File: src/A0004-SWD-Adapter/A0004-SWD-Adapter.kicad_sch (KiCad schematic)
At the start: 13 parts, among them P1 LARGE_SBH11-PBPC-D10-RA-BK_1, P2 SMALL_3220-20-0200-00

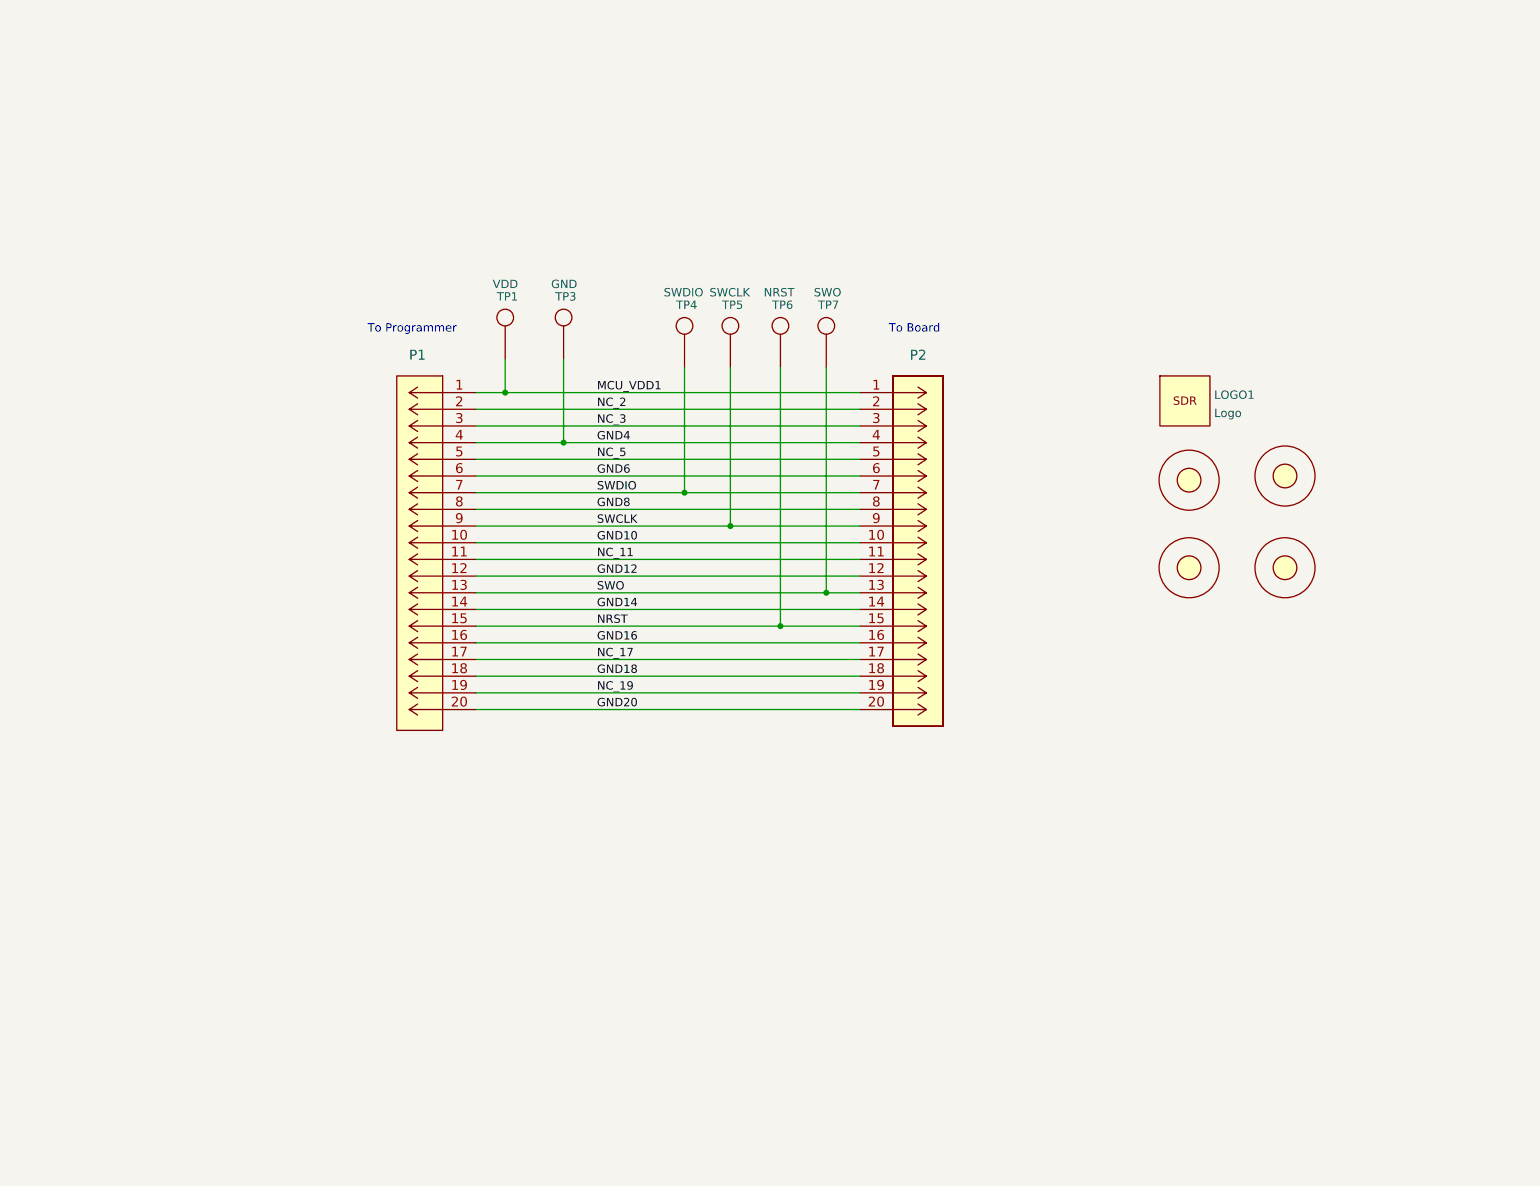
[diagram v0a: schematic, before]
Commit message: implemented schematic with new zenith programmer connectors
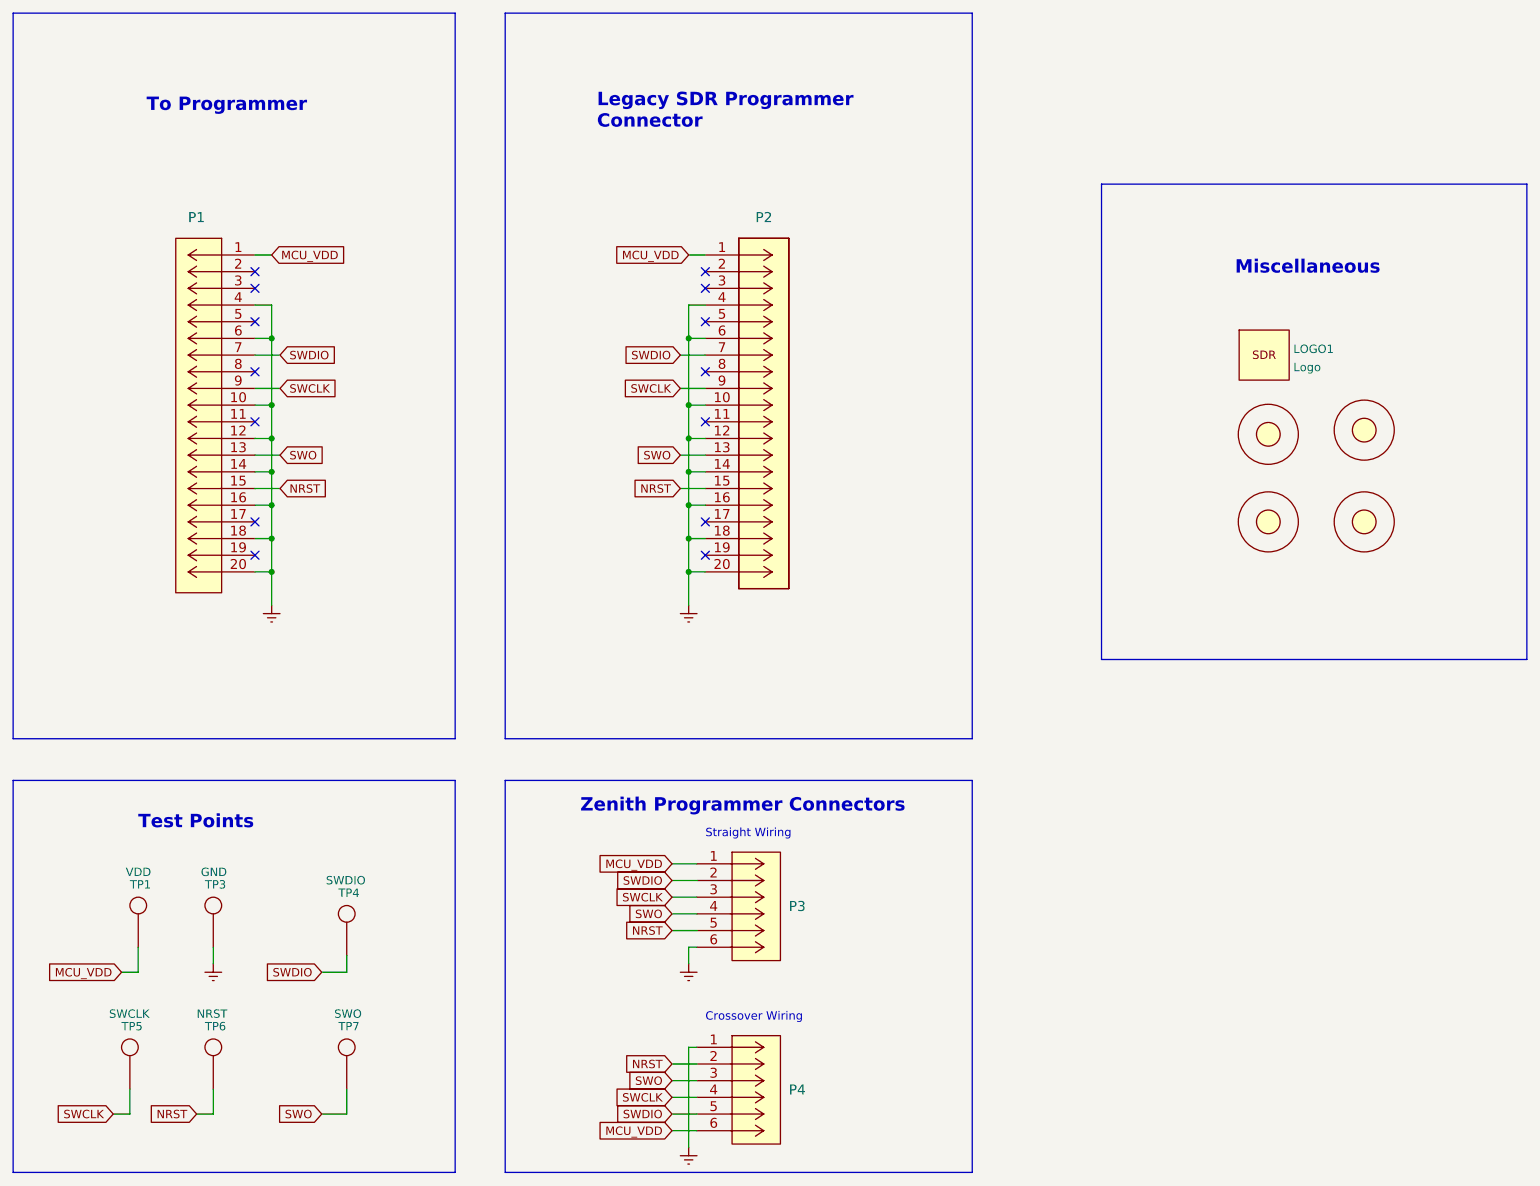
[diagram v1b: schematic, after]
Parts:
- added P3, P4: 0530470610, Full-Flight-Computer:53047-0610, symbol A0004-SWD-Adapter:0530470610
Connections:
- net GND12 is gone; now on net Earth: P1.12, P2.12
- net GND14 is gone; now on net Earth: P1.14, P2.14
- net GND16 is gone; now on net Earth: P1.16, P2.16
- net GND18 is gone; now on net Earth: P1.18, P2.18
- net GND20 is gone; now on net Earth: P1.20, P2.20
- net GND4 is gone; now on net Earth: P1.4, P2.4, TP3.1
- net GND6 is gone; now on net Earth: P1.6, P2.6
- net NRST: now also P3.5, P4.2
- net SWCLK: now also P3.3, P4.4
- net SWDIO: now also P3.2, P4.5
- net SWO: now also P3.4, P4.3
- net GND10 renamed Earth
- net Earth: now also P3.6, P4.1
- net GND8: no longer names the net of P1.8
- net GND8: no longer P2.8
- net MCU_VDD1 renamed MCU_VDD
- net MCU_VDD: now also P3.1, P4.6
- net NC_11: no longer names the net of P1.11
- net NC_11: no longer P2.11
- net NC_17: no longer names the net of P1.17
- net NC_17: no longer P2.17
- net NC_19: no longer names the net of P1.19
- net NC_19: no longer P2.19
- net NC_2: no longer names the net of P1.2
- net NC_2: no longer P2.2
- net NC_3: no longer names the net of P1.3
- net NC_3: no longer P2.3
- net NC_5: no longer names the net of P1.5
- net NC_5: no longer P2.5
- no-connect marks 0 -> 14
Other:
- note added: "Crossover Wiring"
- note added: "Legacy SDR Programmer Connector"
- note added: "Miscellaneous"
- note added: "Straight Wiring"
- note added: "Test Points"
- note added: "Zenith Programmer Connectors"
- note removed: "To Board"
- moved on the sheet: LOGO1, P1, P2, TP1, TP3, TP4, TP5, TP6, TP7

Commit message: routed board with new programmer connectors
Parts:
- removed LOGO1: Logo, A0004-SWD-Adapter:Logo, symbol A0004-SWD-Adapter:Logo
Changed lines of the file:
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@@
     (effects (font (size 1.27 1.27)) (justify left bottom))
   )
-  (text "Miscellaneous" (at 208.915 57.785 0)
+  (text "Miscellaneous" (at 210.82 63.5 0)
     (effects (font (size 2.032 2.032) (thickness 0.4064) bold) (justify left bottom))
   )
@@
         )
       )
-    )
-  )
-  (symbol (lib_id "A0004-SWD-Adapter:Logo") (at 213.36 69.85 0) (unit 1)
-    (in_bom yes) (on_board yes) (dnp no) (fields_autoplaced)
-    (property "Reference" "LOGO1" (at 217.805 68.9415 0)
-      (effects (font (size 1.27 1.27)) (justify left))
-    )
-    (property "Value" "Logo" (at 217.805 71.7166 0)
-      (effects (font (size 1.27 1.27)) (justify left))
-    )
-    (property "Footprint" "A0004-SWD-Adapter:Logo" (at 213.36 69.85 0)
-      (effects (font (size 1.27 1.27)) hide)
-    )
-    (property "Datasheet" "" (at 213.36 69.85 0)
-      (effects (font (size 1.27 1.27)) hide)
-    )
-    (instances
-      (project "A0004-SWD-Adapter"
-        (path "/9102eee1-fd6a-4e1d-8365-191015acf0e6"
-          (reference "LOGO1") (unit 1)
-        )
-      )
